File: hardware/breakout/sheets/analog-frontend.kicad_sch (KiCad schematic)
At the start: 136 parts, among them J19 ACCES I/O USB-AO16-8A mating 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, J20 Photodiode 1 (passive, coax, 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, J21 Photodiode 2 (passive, coax, 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, J22 Microphone (battery-powered, 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, J23 Ambient light sensor (battery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, J24 Accelerometer motion energy (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, J25 Joystick X (battery-powered, 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, J26 Joystick Y (battery-powered, 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, J27 Misc analog input 1 (panel BN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, J28 Misc analog input 1 (panel BN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, J29 Misc analog input 2 (panel BN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, J30 Misc analog input 2 (panel BN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, J31 Misc analog input 3 (panel BN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, J32 Misc analog input 3 (panel BN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, U16 INA105KU, U17 INA105KU, U18 INA105KU, U19 INA105KU, U20 INA105KU, U21 INA105KU, U22 OPA2197IDR, U23 OPA4197IDR, U24 INA105KU, U25 INA105KU, U26 INA105KU, U27 INA105KU, U28 INA105KU, U29 INA105KU, U30 INA105KU

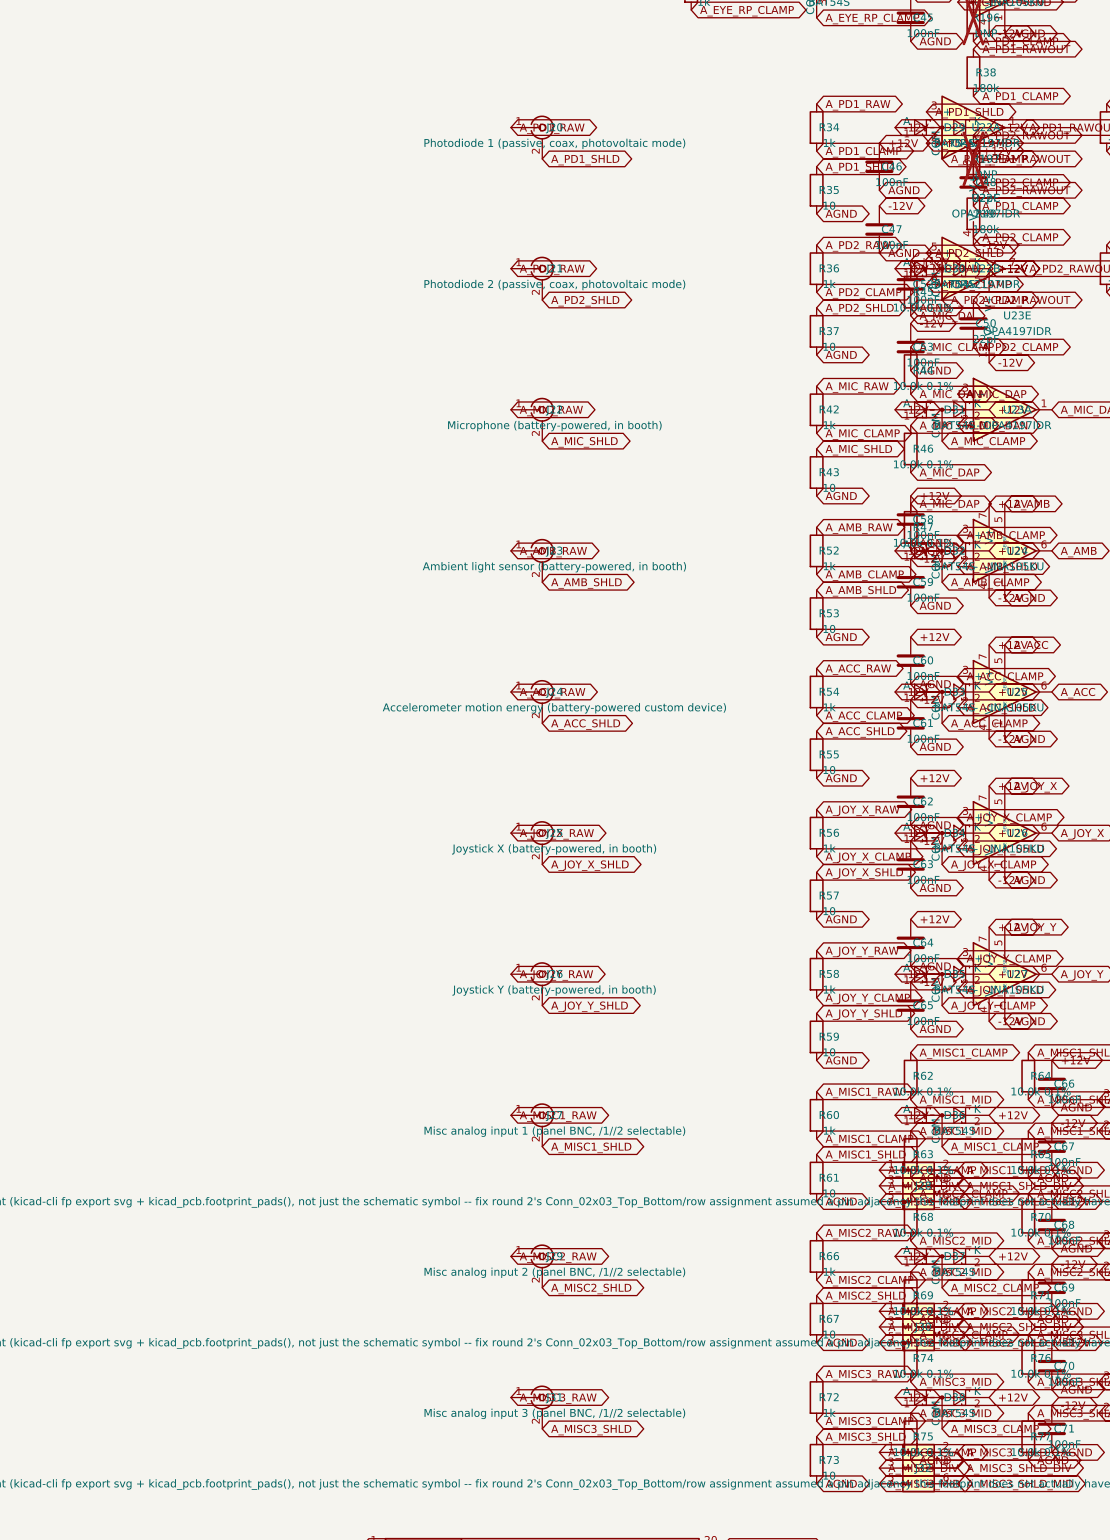
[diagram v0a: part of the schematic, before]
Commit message: fix(hardware): rebuild the connectors on their primary drawings (F6, R1, D3)
Audit step 5, the mechanical half. Three connectors changed, one of them a
fab-stopper, and none of it was visible to the netlist.

MDR68 (the fab-stopper). Rebuilt from MH drawing 3700-0121-01 rev 3.0. The
as-built footprint drilled contacts at 0.5 mm against a required 0.85 mm -- the
pins do not fit, so the board could not have been assembled -- and laid them out
as 2 rows at 2.84 mm where the drawing shows 4 staggered rows of 17 at 1.905 mm.
The 4-row stagger is what makes an 0.85 mm drill manufacturable at a 1.27 mm
mating pitch at all; the array now spans the drawing's own 41.91 mm exactly,
which is the arithmetic that confirms the reading. The claim made during the
audit that it had "no mounting holes at all" was wrong: it had two, Ø2.79 on
57.9 mm centres against the drawing's Ø2.77 on 57.93.

M12 (ruling R1). M12A_5_Panel is deleted, symbol and footprint and generator
function alike. Its contact geometry was sourced well -- IEC 61076-2-101
A-coding, cross-checked three ways -- and it made no difference, because the part
the design procures (Phoenix 1551833) terminates in AWG 22-20 wire and mounts
through the panel. It has no PCB tails, so no board-mount footprint of any
dimensions could have been right, and as built every cable insertion and every
3-4 N.m tightening loaded PCB pads directly. J1 is now a stock 5-way header where
those flying leads land; the connector stays in the order BOM as chassis
furniture.

BNC (F6). BNC_PanelMountable_Vertical puts the connector axis perpendicular to
the PCB -- a 9.65 mm barrel hole through the board -- so on a 430x240 mm board
lying flat in a 2U chassis all 31 barrels pointed at the lid rather than at the
panels. It also cost 5,654 mm2 of pad and 2,267 mm2 of removed copper on every
layer. Replaced by a right-angle dual jack built from Amphenol drawing 31-6575
rev A: 31 ports on 17 bodies, 3 spare ports, every shell still routed
individually.
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
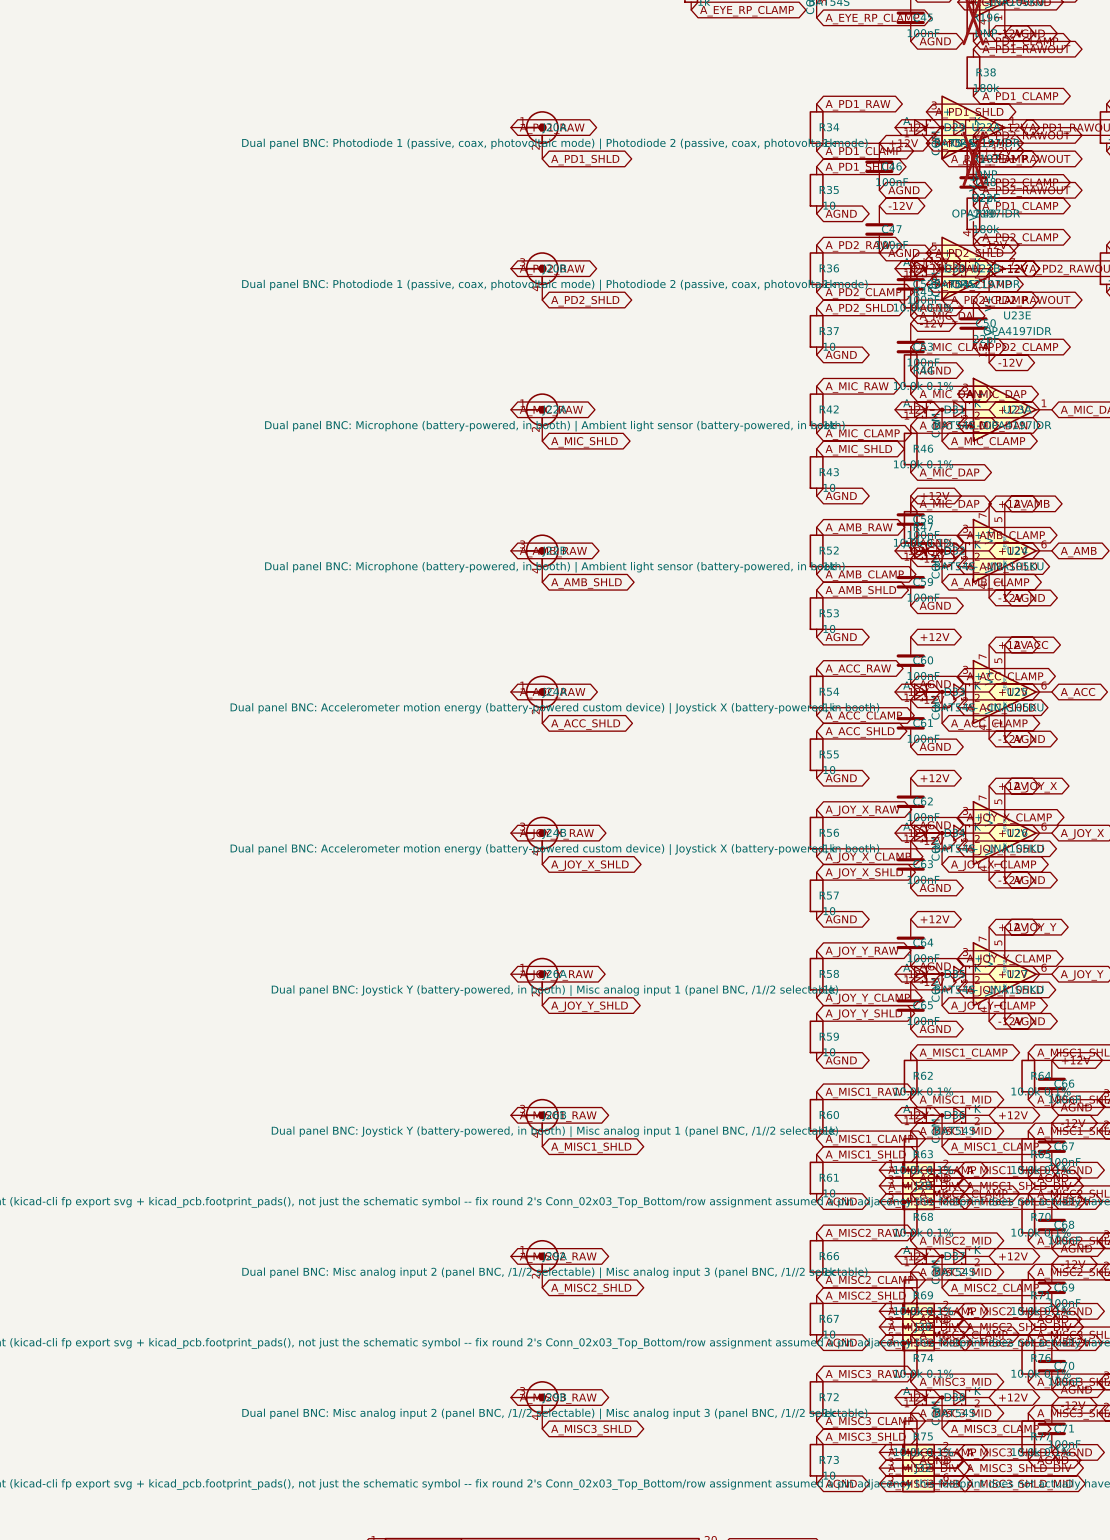
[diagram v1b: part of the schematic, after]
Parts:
- removed J20: Photodiode 1 (passive, coax, photovoltaic mode), Connector_Coaxial:BNC_PanelMountable_Vertical, symbol Connector:Conn_Coaxial
- removed J21: Photodiode 2 (passive, coax, photovoltaic mode), Connector_Coaxial:BNC_PanelMountable_Vertical, symbol Connector:Conn_Coaxial
- removed J22: Microphone (battery-powered, in booth), Connector_Coaxial:BNC_PanelMountable_Vertical, symbol Connector:Conn_Coaxial
- removed J23: Ambient light sensor (battery-powered, in booth), Connector_Coaxial:BNC_PanelMountable_Vertical, symbol Connector:Conn_Coaxial
- removed J24: Accelerometer motion energy (battery-powered cust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, Connector_Coaxial:BNC_PanelMountable_Vertical, symbol Connector:Conn_Coaxial
- removed J25: Joystick X (battery-powered, in booth), Connector_Coaxial:BNC_PanelMountable_Vertical, symbol Connector:Conn_Coaxial
- removed J26: Joystick Y (battery-powered, in booth), Connector_Coaxial:BNC_PanelMountable_Vertical, symbol Connector:Conn_Coaxial
- removed J27: Misc analog input 1 (panel BNC, /1//2 selectable), Connector_Coaxial:BNC_PanelMountable_Vertical, symbol Connector:Conn_Coaxial
- removed J29: Misc analog input 2 (panel BNC, /1//2 selectable), Connector_Coaxial:BNC_PanelMountable_Vertical, symbol Connector:Conn_Coaxial
- removed J31: Misc analog input 3 (panel BNC, /1//2 selectable), Connector_Coaxial:BNC_PanelMountable_Vertical, symbol Connector:Conn_Coaxial
- added J20: Dual panel BNC: Photodiode 1 (passive, coax, phot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, wl-sync:BNC_Dual_RA_Isolated, symbol wl-sync:BNC_Dual_RA_Isolated
- added J22: Dual panel BNC: Microphone (battery-powered, in b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, wl-sync:BNC_Dual_RA_Isolated, symbol wl-sync:BNC_Dual_RA_Isolated
- added J24: Dual panel BNC: Accelerometer motion energy (batt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, wl-sync:BNC_Dual_RA_Isolated, symbol wl-sync:BNC_Dual_RA_Isolated
- added J26: Dual panel BNC: Joystick Y (battery-powered, in b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, wl-sync:BNC_Dual_RA_Isolated, symbol wl-sync:BNC_Dual_RA_Isolated
- added J29: Dual panel BNC: Misc analog input 2 (panel BNC, /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, wl-sync:BNC_Dual_RA_Isolated, symbol wl-sync:BNC_Dual_RA_Isolated
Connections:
- net A_ACC_RAW: now also J24.1 (A_In)
- net A_ACC_SHLD: now also J24.2 (A_Ext)
- net A_AMB_RAW: now also J22.3 (B_In)
- net A_AMB_SHLD: now also J22.4 (B_Ext)
- net A_JOY_X_RAW: now also J24.3 (B_In)
- net A_JOY_X_SHLD: now also J24.4 (B_Ext)
- net A_JOY_Y_RAW: now also J26.1 (A_In)
- net A_JOY_Y_SHLD: now also J26.2 (A_Ext)
- net A_MIC_RAW: now also J22.1 (A_In)
- net A_MIC_SHLD: now also J22.2 (A_Ext)
- net A_MISC1_RAW: now also J26.3 (B_In)
- net A_MISC1_SHLD: now also J26.4 (B_Ext)
- net A_MISC2_RAW: now also J29.1 (A_In)
- net A_MISC2_SHLD: now also J29.2 (A_Ext)
- net A_MISC3_RAW: now also J29.3 (B_In)
- net A_MISC3_SHLD: now also J29.4 (B_Ext)
- net A_PD1_RAW: now also J20.1 (A_In)
- net A_PD1_SHLD: now also J20.2 (A_Ext)
- net A_PD2_RAW: now also J20.3 (B_In)
- net A_PD2_SHLD: now also J20.4 (B_Ext)
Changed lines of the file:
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@@
 	)
 	(symbol
-		(lib_id "Connector:Conn_Coaxial")
+		(lib_id "wl-sync:BNC_Dual_RA_Isolated")
 		(at 20.32 157.48 0)
 		(unit 1)
@@
 			(effects (font (size 1.27 1.27)))
 		)
-		(property "Value" "Photodiode 1 (passive, coax, photovoltaic mode)"
+		(property "Value" "Dual panel BNC: Photodiode 1 (passive, coax, photovoltaic mode) | Photodiode 2 (passive, coax, photovoltaic mode)"
 			(at 22.352 160.01999999999998 0)
 			(effects (font (size 1.27 1.27)))
 		)
-		(property "Footprint" "Connector_Coaxial:BNC_PanelMountable_Vertical"
+		(property "Footprint" "wl-sync:BNC_Dual_RA_Isolated"
 			(at 20.32 157.48 0)
 			(effects (font (size 1.27 1.27)) (hide yes))
@@
 	)
 	(symbol
-		(lib_id "Connector:Conn_Coaxial")
+		(lib_id "wl-sync:BNC_Dual_RA_Isolated")
 		(at 20.32 180.33999999999997 0)
-		(unit 1)
+		(unit 2)
 		(exclude_from_sim no)
 		(in_bom yes)
 		(on_board yes)
 		(dnp no)
-		(property "Reference" "J21"
+		(property "Reference" "J20"
 			(at 22.352 180.33999999999997 0)
 			(effects (font (size 1.27 1.27)))
 		)
-		(property "Value" "Photodiode 2 (passive, coax, photovoltaic mode)"
+		(property "Value" "Dual panel BNC: Photodiode 1 (passive, coax, photovoltaic mode) | Photodiode 2 (passive, coax, photovoltaic mode)"
 			(at 22.352 182.87999999999997 0)
 			(effects (font (size 1.27 1.27)))
 		)
-		(property "Footprint" "Connector_Coaxial:BNC_PanelMountable_Vertical"
+		(property "Footprint" "wl-sync:BNC_Dual_RA_Isolated"
 			(at 20.32 180.33999999999997 0)
 			(effects (font (size 1.27 1.27)) (hide yes))
@@
 			(effects (font (size 1.27 1.27)) (hide yes))
 		)
-		(pin "1")
-		(pin "2")
+		(pin "3")
+		(pin "4")
 		(instances
 			(project "breakout"
 				(path "/d2c4d978-5db4-46d9-a1cd-a7af0aeb1700/224d9c0c-248e-4691-aa68-8b342525837c"
-					(reference "J21") (unit 1)
+					(reference "J20") (unit 2)
 				)
 			)
@@
 	)
 	(symbol
-		(lib_id "Connector:Conn_Coaxial")
+		(lib_id "wl-sync:BNC_Dual_RA_Isolated")
 		(at 20.32 203.2 0)
 		(unit 1)
@@
 			(effects (font (size 1.27 1.27)))
 		)
-		(property "Value" "Microphone (battery-powered, in booth)"
+		(property "Value" "Dual panel BNC: Microphone (battery-powered, in booth) | Ambient light sensor (battery-powered, in booth)"
 			(at 22.352 205.73999999999998 0)
 			(effects (font (size 1.27 1.27)))
 		)
-		(property "Footprint" "Connector_Coaxial:BNC_PanelMountable_Vertical"
+		(property "Footprint" "wl-sync:BNC_Dual_RA_Isolated"
 			(at 20.32 203.2 0)
 			(effects (font (size 1.27 1.27)) (hide yes))
@@
 	)
 	(symbol
-		(lib_id "Connector:Conn_Coaxial")
+		(lib_id "wl-sync:BNC_Dual_RA_Isolated")
 		(at 20.32 226.06 0)
-		(unit 1)
+		(unit 2)
 		(exclude_from_sim no)
 		(in_bom yes)
 		(on_board yes)
 		(dnp no)
-		(property "Reference" "J23"
+		(property "Reference" "J22"
 			(at 22.352 226.06 0)
 			(effects (font (size 1.27 1.27)))
 		)
-		(property "Value" "Ambient light sensor (battery-powered, in booth)"
+		(property "Value" "Dual panel BNC: Microphone (battery-powered, in booth) | Ambient light sensor (battery-powered, in booth)"
 			(at 22.352 228.6 0)
 			(effects (font (size 1.27 1.27)))
 		)
-		(property "Footprint" "Connector_Coaxial:BNC_PanelMountable_Vertical"
+		(property "Footprint" "wl-sync:BNC_Dual_RA_Isolated"
 			(at 20.32 226.06 0)
 			(effects (font (size 1.27 1.27)) (hide yes))
@@
 			(effects (font (size 1.27 1.27)) (hide yes))
 		)
-		(pin "1")
-		(pin "2")
+		(pin "3")
+		(pin "4")
 		(instances
 			(project "breakout"
 				(path "/d2c4d978-5db4-46d9-a1cd-a7af0aeb1700/224d9c0c-248e-4691-aa68-8b342525837c"
-					(reference "J23") (unit 1)
+					(reference "J22") (unit 2)
 				)
 			)
@@
 	)
 	(symbol
-		(lib_id "Connector:Conn_Coaxial")
+		(lib_id "wl-sync:BNC_Dual_RA_Isolated")
 		(at 20.32 248.92 0)
 		(unit 1)
@@
 			(effects (font (size 1.27 1.27)))
 		)
-		(property "Value" "Accelerometer motion energy (battery-powered custom device)"
+		(property "Value" "Dual panel BNC: Accelerometer motion energy (battery-powered custom device) | Joystick X (battery-powered, in booth)"
 			(at 22.352 251.45999999999998 0)
 			(effects (font (size 1.27 1.27)))
 		)
-		(property "Footprint" "Connector_Coaxial:BNC_PanelMountable_Vertical"
+		(property "Footprint" "wl-sync:BNC_Dual_RA_Isolated"
 			(at 20.32 248.92 0)
 			(effects (font (size 1.27 1.27)) (hide yes))
@@
 	)
 	(symbol
-		(lib_id "Connector:Conn_Coaxial")
+		(lib_id "wl-sync:BNC_Dual_RA_Isolated")
 		(at 20.32 271.78 0)
-		(unit 1)
+		(unit 2)
 		(exclude_from_sim no)
 		(in_bom yes)
 		(on_board yes)
 		(dnp no)
-		(property "Reference" "J25"
+		(property "Reference" "J24"
 			(at 22.352 271.78 0)
 			(effects (font (size 1.27 1.27)))
 		)
-		(property "Value" "Joystick X (battery-powered, in booth)"
+		(property "Value" "Dual panel BNC: Accelerometer motion energy (battery-powered custom device) | Joystick X (battery-powered, in booth)"
 			(at 22.352 274.32 0)
 			(effects (font (size 1.27 1.27)))
 		)
-		(property "Footprint" "Connector_Coaxial:BNC_PanelMountable_Vertical"
+		(property "Footprint" "wl-sync:BNC_Dual_RA_Isolated"
 			(at 20.32 271.78 0)
 			(effects (font (size 1.27 1.27)) (hide yes))
@@
 			(effects (font (size 1.27 1.27)) (hide yes))
 		)
-		(pin "1")
-		(pin "2")
+		(pin "3")
+		(pin "4")
 		(instances
 			(project "breakout"
 				(path "/d2c4d978-5db4-46d9-a1cd-a7af0aeb1700/224d9c0c-248e-4691-aa68-8b342525837c"
-					(reference "J25") (unit 1)
+					(reference "J24") (unit 2)
 				)
 			)
@@
 	)
 	(symbol
-		(lib_id "Connector:Conn_Coaxial")
+		(lib_id "wl-sync:BNC_Dual_RA_Isolated")
 		(at 20.32 294.64 0)
 		(unit 1)
@@
 			(effects (font (size 1.27 1.27)))
 		)
-		(property "Value" "Joystick Y (battery-powered, in booth)"
+		(property "Value" "Dual panel BNC: Joystick Y (battery-powered, in booth) | Misc analog input 1 (panel BNC, /1//2 selectable)"
 			(at 22.352 297.18 0)
 			(effects (font (size 1.27 1.27)))
 		)
-		(property "Footprint" "Connector_Coaxial:BNC_PanelMountable_Vertical"
+		(property "Footprint" "wl-sync:BNC_Dual_RA_Isolated"
 			(at 20.32 294.64 0)
 			(effects (font (size 1.27 1.27)) (hide yes))
@@
 	)
 	(symbol
-		(lib_id "Connector:Conn_Coaxial")
+		(lib_id "wl-sync:BNC_Dual_RA_Isolated")
 		(at 20.32 317.5 0)
-		(unit 1)
+		(unit 2)
 		(exclude_from_sim no)
 		(in_bom yes)
 		(on_board yes)
 		(dnp no)
-		(property "Reference" "J27"
+		(property "Reference" "J26"
 			(at 22.352 317.5 0)
 			(effects (font (size 1.27 1.27)))
 		)
-		(property "Value" "Misc analog input 1 (panel BNC, /1//2 selectable)"
+		(property "Value" "Dual panel BNC: Joystick Y (battery-powered, in booth) | Misc analog input 1 (panel BNC, /1//2 selectable)"
 			(at 22.352 320.04 0)
 			(effects (font (size 1.27 1.27)))
 		)
-		(property "Footprint" "Connector_Coaxial:BNC_PanelMountable_Vertical"
+		(property "Footprint" "wl-sync:BNC_Dual_RA_Isolated"
 			(at 20.32 317.5 0)
 			(effects (font (size 1.27 1.27)) (hide yes))
@@
 			(effects (font (size 1.27 1.27)) (hide yes))
 		)
-		(pin "1")
-		(pin "2")
+		(pin "3")
+		(pin "4")
 		(instances
 			(project "breakout"
 				(path "/d2c4d978-5db4-46d9-a1cd-a7af0aeb1700/224d9c0c-248e-4691-aa68-8b342525837c"
-					(reference "J27") (unit 1)
+					(reference "J26") (unit 2)
 				)
 			)
@@
 	)
 	(symbol
-		(lib_id "Connector:Conn_Coaxial")
+		(lib_id "wl-sync:BNC_Dual_RA_Isolated")
 		(at 20.32 340.35999999999996 0)
 		(unit 1)
@@
 			(effects (font (size 1.27 1.27)))
 		)
-		(property "Value" "Misc analog input 2 (panel BNC, /1//2 selectable)"
+		(property "Value" "Dual panel BNC: Misc analog input 2 (panel BNC, /1//2 selectable) | Misc analog input 3 (panel BNC, /1//2 selectable)"
 			(at 22.352 342.9 0)
 			(effects (font (size 1.27 1.27)))
 		)
-		(property "Footprint" "Connector_Coaxial:BNC_PanelMountable_Vertical"
+		(property "Footprint" "wl-sync:BNC_Dual_RA_Isolated"
 			(at 20.32 340.35999999999996 0)
 			(effects (font (size 1.27 1.27)) (hide yes))
@@
 	)
 	(symbol
-		(lib_id "Connector:Conn_Coaxial")
+		(lib_id "wl-sync:BNC_Dual_RA_Isolated")
 		(at 20.32 363.21999999999997 0)
-		(unit 1)
+		(unit 2)
 		(exclude_from_sim no)
 		(in_bom yes)
 		(on_board yes)
 		(dnp no)
-		(property "Reference" "J31"
+		(property "Reference" "J29"
 			(at 22.352 363.21999999999997 0)
 			(effects (font (size 1.27 1.27)))
 		)
-		(property "Value" "Misc analog input 3 (panel BNC, /1//2 selectable)"
+		(property "Value" "Dual panel BNC: Misc analog input 2 (panel BNC, /1//2 selectable) | Misc analog input 3 (panel BNC, /1//2 selectable)"
 			(at 22.352 365.76 0)
 			(effects (font (size 1.27 1.27)))
 		)
-		(property "Footprint" "Connector_Coaxial:BNC_PanelMountable_Vertical"
+		(property "Footprint" "wl-sync:BNC_Dual_RA_Isolated"
 			(at 20.32 363.21999999999997 0)
 			(effects (font (size 1.27 1.27)) (hide yes))
@@
 			(effects (font (size 1.27 1.27)) (hide yes))
 		)
-		(pin "1")
-		(pin "2")
+		(pin "3")
+		(pin "4")
 		(instances
 			(project "breakout"
 				(path "/d2c4d978-5db4-46d9-a1cd-a7af0aeb1700/224d9c0c-248e-4691-aa68-8b342525837c"
-					(reference "J31") (unit 1)
+					(reference "J29") (unit 2)
 				)
 			)
